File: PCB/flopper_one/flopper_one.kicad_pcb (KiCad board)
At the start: 2 copper layers, 76.8 x 63 mm, 23 parts, among them J1 To PN532 ->, J2 <- ST7789, Q1 2N2219, SW1 SW_Omron_B3FS, SW2 SW_Omron_B3FS, SW3 SW_Omron_B3FS, SW4 SW_Omron_B3FS, SW5 SW_Omron_B3FS, SW6 SW_SPST, U1 TP4056-42-ESOP8, U4 hw-045

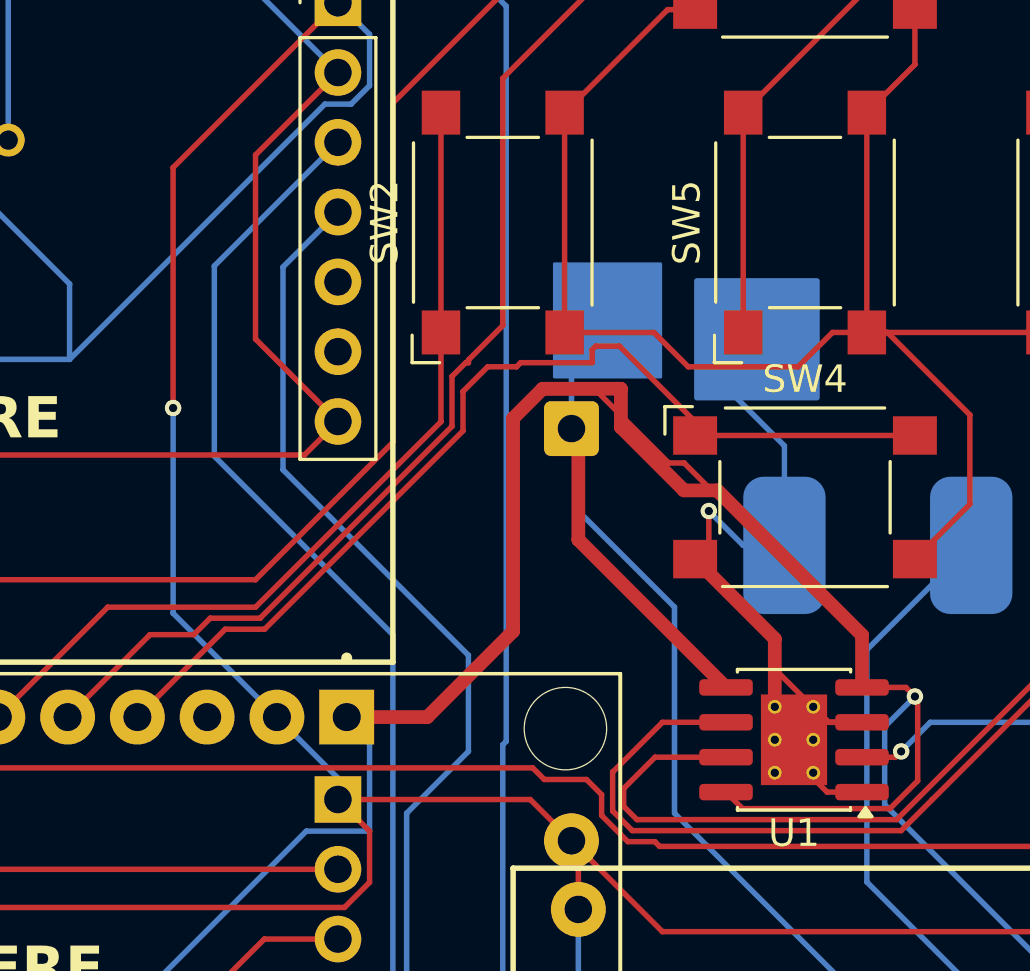
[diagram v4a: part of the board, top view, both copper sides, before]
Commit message: rm that one resistor + gnd pour
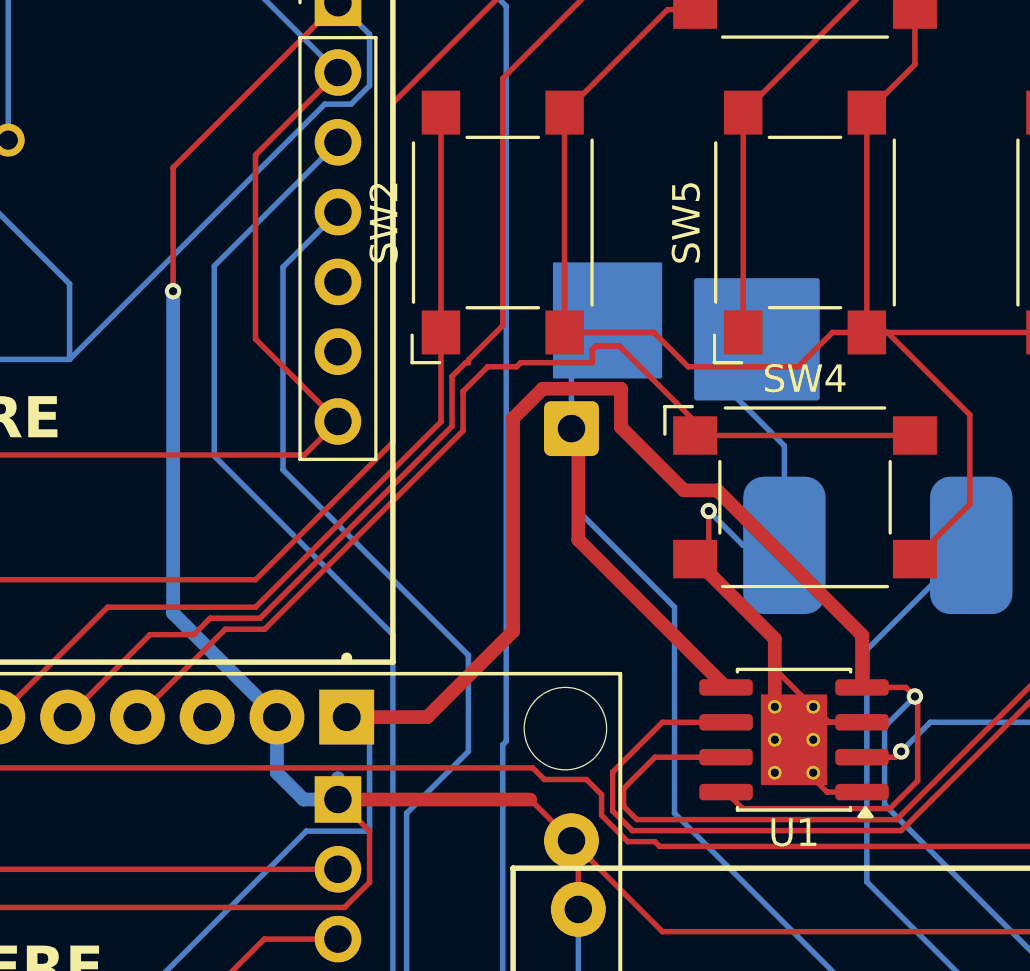
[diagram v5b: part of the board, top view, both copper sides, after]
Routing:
- net /CE: track 167.2 -> 151.9 mm
- net GND: track 373.3 -> 374.8 mm
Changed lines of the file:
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@@
-	)
-	(segment
-		(start 68 39.25)
-		(end 68 48)
-		(width 0.2)
-		(layer "F.Cu")
-		(net 3)
 	)
 	(segment
@@
 		(start 74 62.25)
 		(end 81 62.25)
-		(width 0.2)
+		(width 0.5)
 		(layer "F.Cu")
 		(net 3)
@@
 	)
 	(segment
+		(start 68 39.25)
+		(end 68 43.75)
+		(width 0.2)
+		(layer "F.Cu")
+		(net 3)
+	)
+	(segment
 		(start 98 30.5)
 		(end 98 27.25)
@@
 	)
 	(via
-		(at 68 48)
+		(at 68 43.75)
 		(size 0.6)
 		(drill 0.3)
@@
 	)
 	(segment
+		(start 68 43.75)
+		(end 68 55.47)
+		(width 0.5)
+		(layer "B.Cu")
+		(net 3)
+	)
+	(segment
 		(start 90.25 49.375)
 		(end 90.25 53)
@@
 	)
 	(segment
+		(start 68 55.47)
+		(end 71.78 59.25)
+		(width 0.5)
+		(layer "B.Cu")
+		(net 3)
+	)
+	(segment
 		(start 103.051 85.538892)
 		(end 102.288892 86.301)
@@
 		(start 74 61.47)
 		(end 74 62.25)
-		(width 0.2)
+		(width 0.5)
 		(layer "B.Cu")
 		(net 3)
@@
 	)
 	(segment
-		(start 68 55.47)
-		(end 71.78 59.25)
-		(width 0.2)
-		(layer "B.Cu")
-		(net 3)
-	)
-	(segment
 		(start 87.28616 83.5)
 		(end 82.75 78.96384)
@@
 	)
 	(segment
-		(start 68 48)
-		(end 68 55.47)
-		(width 0.2)
-		(layer "B.Cu")
-		(net 3)
-	)
-	(segment
 		(start 90.25 53)
 		(end 88.75 53)
@@
 	)
 	(segment
+		(start 72.75 62.25)
+		(end 71.78 61.28)
+		(width 0.5)
+		(layer "B.Cu")
+		(net 3)
+	)
+	(segment
+		(start 74 62.25)
+		(end 72.75 62.25)
+		(width 0.5)
+		(layer "B.Cu")
+		(net 3)
+	)
+	(segment
 		(start 64.23324 46.231)
 		(end 73.52324 36.941)
@@
 	)
 	(segment
-		(start 71.78 59.25)
-		(end 74 61.47)
-		(width 0.2)
-		(layer "B.Cu")
-		(net 3)
-	)
-	(segment
 		(start 105.661 73.497471)
 		(end 103.051 76.107471)
@@
 		(end 59.46 38.71)
 		(width 0.2)
+		(layer "B.Cu")
+		(net 3)
+	)
+	(segment
+		(start 71.78 61.28)
+		(end 71.78 59.25)
+		(width 0.5)
 		(layer "B.Cu")
 		(net 3)
@@
 	)
 	(segment
-		(start 86.03716 50.001)
-		(end 83.48516 47.449)
-		(width 0.2)
-		(layer "F.Cu")
-		(net 41)
-	)
-	(segment
 		(start 94.67 58.17)
 		(end 93.075 58.17)
@@
 		(start 88.726 62.581)
 		(end 88.125 61.98)
-		(width 0.2)
-		(layer "F.Cu")
-		(net 41)
-	)
-	(segment
-		(start 83.48516 47.449)
-		(end 81.51484 47.449)
 		(width 0.2)
 		(layer "F.Cu")
@@
 	)
 	(segment
-		(start 93.075 56.475057)
-		(end 86.600943 50.001)
-		(width 0.2)
-		(layer "F.Cu")
-		(net 41)
-	)
-	(segment
 		(start 81.76484 79.949)
 		(end 81.71384 80)
-		(width 0.2)
-		(layer "F.Cu")
-		(net 41)
-	)
-	(segment
-		(start 86.600943 50.001)
-		(end 86.03716 50.001)
 		(width 0.2)
 		(layer "F.Cu")
@@
 			)
 		)
+	)
+	(zone
+		(net 0)
+		(net_name "")
+		(layers "F.Cu" "B.Cu")
+		(hatch edge 0.5)
+		(connect_pads
+			(clearance 0)
+		)
+		(min_thickness 0.25)
+		(filled_areas_thickness no)
+		(keepout
+			(tracks allowed)
+			(vias allowed)
+			(pads allowed)
+			(copperpour not_allowed)
+			(footprints allowed)
+		)
+		(placement
+			(enabled no)
+			(sheetname "/")
+		)
+		(fill
+			(thermal_gap 0.5)
+			(thermal_bridge_width 0.5)
+		)
+		(polygon
+			(pts
+				(xy 33 45.25) (xy 76 45.25) (xy 75.75 87.25) (xy 33 87.25)
+			)
+		)

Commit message: make more things thicker
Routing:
- net GND: track 374.8 -> 360.8 mm
- net /CE: track 151.9 -> 154.4 mm, vias 3 -> 1
- net /SDA2: vias 0 -> 1
- net Net-(U2-GPIO23): vias 0 -> 1
- net /SCL2: vias 0 -> 1
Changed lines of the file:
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@@
-	)
-	(segment
-		(start 74 61.47)
-		(end 74 62.25)
-		(width 0.5)
-		(layer "B.Cu")
-		(net 3)
 	)
 	(segment
@@
 	)
 	(segment
-		(start 102.288892 86.301)
-		(end 93.051 86.301)
-		(width 0.2)
-		(layer "B.Cu")
-		(net 3)
-	)
-	(segment
 		(start 103.051 76.107471)
 		(end 103.051 85.538892)
@@
 	)
 	(segment
-		(start 93.051 86.301)
-		(end 90.25 83.5)
-		(width 0.2)
-		(layer "B.Cu")
-		(net 3)
-	)
-	(segment
 		(start 44.54 28.2771)
 		(end 44.54 28)
@@
 	)
 	(segment
+		(start 61.62 84.63)
+		(end 71.615 74.635)
+		(width 0.2)
+		(layer "F.Cu")
+		(net 11)
+	)
+	(segment
+		(start 71.615 74.635)
+		(end 71.635 74.635)
+		(width 0.2)
+		(layer "F.Cu")
+		(net 11)
+	)
+	(segment
+		(start 61.62 84.65)
+		(end 61.62 84.63)
+		(width 0.2)
+		(layer "F.Cu")
+		(net 11)
+	)
+	(via
+		(at 71.635 74.635)
+		(size 0.6)
+		(drill 0.3)
+		(layers "F.Cu" "B.Cu")
+		(net 11)
+	)
+	(segment
 		(start 78.75 60.5)
 		(end 78.75 57)
@@
 	(segment
 		(start 72 74.27)
-		(end 61.62 84.65)
+		(end 71.635 74.635)
 		(width 0.2)
 		(layer "B.Cu")
@@
 	)
 	(segment
+		(start 59.08 84.65)
+		(end 70.865 72.865)
+		(width 0.2)
+		(layer "F.Cu")
+		(net 12)
+	)
+	(via
+		(at 70.865 72.865)
+		(size 0.6)
+		(drill 0.3)
+		(layers "F.Cu" "B.Cu")
+		(net 12)
+	)
+	(segment
 		(start 71.48 72.25)
-		(end 59.08 84.65)
+		(end 70.865 72.865)
 		(width 0.2)
 		(layer "B.Cu")
@@
 		(end 80 78.97)
 		(width 0.2)
-		(layer "B.Cu")
+		(layer "F.Cu")
+		(net 15)
+	)
+	(via
+		(at 80 78.97)
+		(size 0.6)
+		(drill 0.3)
+		(layers "F.Cu" "B.Cu")
 		(net 15)
 	)
@@
 	)
 	(segment
-		(start 98.949 82.949)
+		(start 98.799 81.049)
+		(end 101 83.25)
+		(width 0.5)
+		(layer "B.Cu")
+		(net 39)
+	)
+	(segment
+		(start 98.949 75.449)
+		(end 98.799 75.599)
+		(width 0.5)
+		(layer "B.Cu")
+		(net 39)
+	)
+	(segment
+		(start 101 83.25)
 		(end 101 85)
-		(width 0.2)
+		(width 0.5)
 		(layer "B.Cu")
 		(net 39)
@@
 		(start 82.75 51.75)
 		(end 86.25 55.25)
-		(width 0.2)
+		(width 0.5)
 		(layer "B.Cu")
 		(net 39)
@@
 	)
 	(segment
+		(start 98.799 75.599)
+		(end 98.799 81.049)
+		(width 0.5)
+		(layer "B.Cu")
+		(net 39)
+	)
+	(segment
 		(start 82.5 45.8125)
 		(end 82.5 48.75)
-		(width 0.2)
+		(width 0.5)
 		(layer "B.Cu")
 		(net 39)
@@
 		(start 86.25 55.25)
 		(end 86.25 62.75)
-		(width 0.2)
+		(width 0.5)
 		(layer "B.Cu")
 		(net 39)
@@
 	)
 	(segment
-		(start 98.949 75.449)
-		(end 98.949 82.949)
-		(width 0.2)
-		(layer "B.Cu")
-		(net 39)
-	)
-	(segment
 		(start 86.25 62.75)
 		(end 98.949 75.449)
-		(width 0.2)
+		(width 0.5)
 		(layer "B.Cu")
 		(net 39)
@@
 		(start 82.75 49)
 		(end 82.75 51.75)
-		(width 0.2)
+		(width 0.5)
 		(layer "B.Cu")
 		(net 39)
@@
 		(start 93.25 65.25)
 		(end 93.25 56.8)
-		(width 0.2)
+		(width 0.5)
 		(layer "B.Cu")
 		(net 40)
@@
 		(start 101 73)
 		(end 93.25 65.25)
-		(width 0.2)
+		(width 0.5)
 		(layer "B.Cu")
 		(net 40)
@@
 		(start 101 80)
 		(end 101 73)
-		(width 0.2)
+		(width 0.5)
 		(layer "B.Cu")
 		(net 40)
@@
 		(start 93.25 56.8)
 		(end 97.05 53)
-		(width 0.2)
+		(width 0.5)
 		(layer "B.Cu")
 		(net 40)
-	)
-	(segment
-		(start 86.699 80)
-		(end 83.78616 80)
-		(width 0.2)
-		(layer "F.Cu")
-		(net 41)
-	)
-	(segment
-		(start 72.75 80)
-		(end 67.5 74.75)
-		(width 0.2)
-		(layer "F.Cu")
-		(net 41)
 	)
 	(segment
@@
 	)
 	(segment
-		(start 83.73516 79.949)
-		(end 81.76484 79.949)
-		(width 0.2)
-		(layer "F.Cu")
-		(net 41)
-	)
-	(segment
 		(start 95 58.5)
 		(end 94.67 58.17)
@@
 	)
 	(segment
-		(start 86.75 79.949)
-		(end 86.699 80)
-		(width 0.2)
-		(layer "F.Cu")
-		(net 41)
-	)
-	(segment
-		(start 81.76484 79.949)
-		(end 81.71384 80)
-		(width 0.2)
-		(layer "F.Cu")
-		(net 41)
-	)
-	(segment
 		(start 104.46 73)
 		(end 104.46 80)
@@
 	)
 	(segment
-		(start 83.78616 80)
-		(end 83.73516 79.949)
-		(width 0.2)
-		(layer "F.Cu")
-		(net 41)
-	)
-	(segment
 		(start 82.801 81.301)
 		(end 103.659 81.301)
 		(width 0.2)
 		(layer "F.Cu")
-		(net 41)
-	)
-	(segment
-		(start 81.71384 80)
-		(end 72.75 80)
-		(width 0.2)
-		(layer "F.Cu")
-		(net 41)
-	)
-	(via
-		(at 86.75 79.949)
-		(size 0.6)
-		(drill 0.3)
-		(layers "F.Cu" "B.Cu")
-		(net 41)
-	)
-	(via
-		(at 67.5 74.75)
-		(size 0.6)
-		(drill 0.3)
-		(layers "F.Cu" "B.Cu")
 		(net 41)
 	)
@@
 	)
 	(segment
+		(start 70.551 71.699)
+		(end 69.375 72.875)
+		(width 0.5)
+		(layer "B.Cu")
+		(net 41)
+	)
+	(segment
 		(start 93.899 59.601)
 		(end 95 58.5)
@@
 	)
 	(segment
+		(start 74.25 71.699)
+		(end 70.551 71.699)
+		(width 0.5)
+		(layer "B.Cu")
+		(net 41)
+	)
+	(segment
+		(start 75.449 70.5)
+		(end 74.25 71.699)
+		(width 0.5)
+		(layer "B.Cu")
+		(net 41)
+	)
+	(segment
+		(start 79.201 86.451)
+		(end 94.099 86.451)
+		(width 0.5)
+		(layer "B.Cu")
+		(net 41)
+	)
+	(segment
+		(start 69.375 72.875)
+		(end 69.375 76.625)
+		(width 0.5)
+		(layer "B.Cu")
+		(net 41)
+	)
+	(segment
+		(start 94.099 86.451)
+		(end 97.05 83.5)
+		(width 0.5)
+		(layer "B.Cu")
+		(net 41)
+	)
+	(segment
+		(start 75.151 60.151)
+		(end 74.75 59.75)
+		(width 0.5)
+		(layer "B.Cu")
+		(net 41)
+	)
+	(segment
 		(start 104.46 73)
 		(end 93.899 62.439)
@@
 	)
 	(segment
-		(start 75.151 60.081)
-		(end 74.32 59.25)
-		(width 0.2)
-		(layer "B.Cu")
-		(net 41)
-	)
-	(segment
-		(start 86.75 79.949)
-		(end 93.499 79.949)
-		(width 0.2)
+		(start 75.449 60.379)
+		(end 75.449 70.5)
+		(width 0.5)
 		(layer "B.Cu")
 		(net 41)
@@
 	)
 	(segment
-		(start 67.5 74.75)
-		(end 67.5 68.75)
-		(width 0.2)
-		(layer "B.Cu")
-		(net 41)
-	)
-	(segment
-		(start 75.151 63.401)
-		(end 75.151 60.081)
-		(width 0.2)
-		(layer "B.Cu")
-		(net 41)
-	)
-	(segment
-		(start 72.849 63.401)
-		(end 75.151 63.401)
-		(width 0.2)
-		(layer "B.Cu")
-		(net 41)
-	)
-	(segment
-		(start 67.5 68.75)
-		(end 72.849 63.401)
-		(width 0.2)
-		(layer "B.Cu")
-		(net 41)
-	)
-	(segment
-		(start 93.499 79.949)
-		(end 97.05 83.5)
-		(width 0.2)
-		(layer "B.Cu")
-		(net 41)
+		(start 74.32 59.25)
+		(end 75.449 60.379)
+		(width 0.5)
+		(layer "B.Cu")
+		(net 41)
+	)
+	(segment
+		(start 69.375 76.625)
+		(end 79.201 86.451)
+		(width 0.5)
+		(layer "B.Cu")
+		(net 41)
